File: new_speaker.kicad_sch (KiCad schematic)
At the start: 11 parts, among them J1 Conn_01x02, J2 Conn_01x04_Pin, J3 Conn_01x03_Pin, U1 MAX98357A

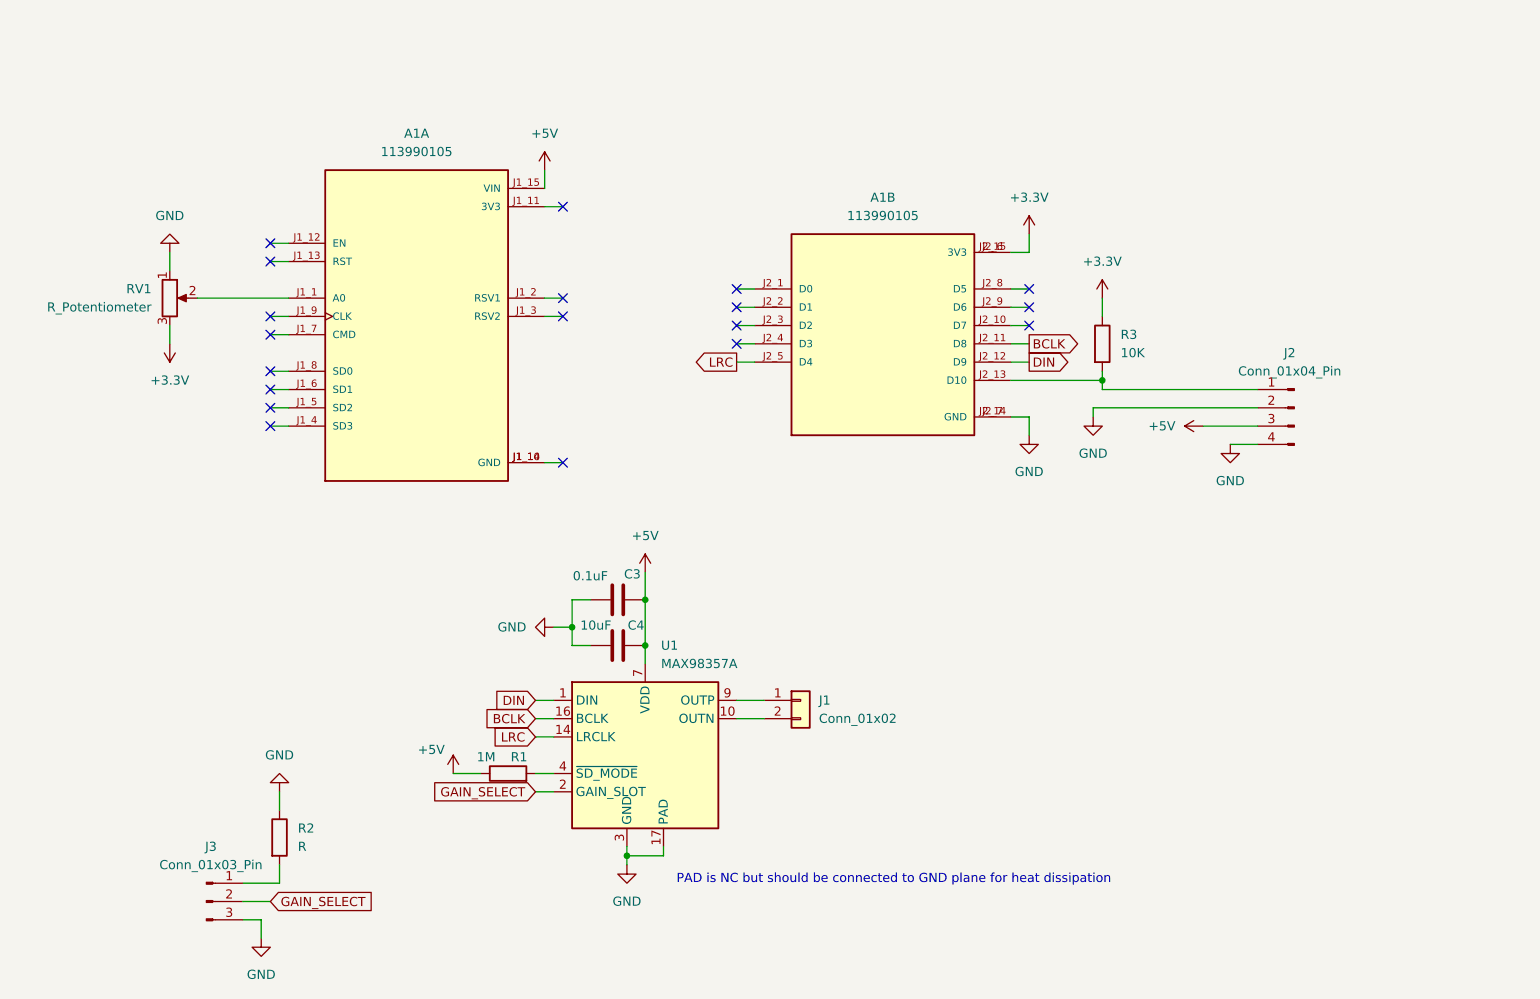
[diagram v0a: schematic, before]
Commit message: fixed nodemcu footprint
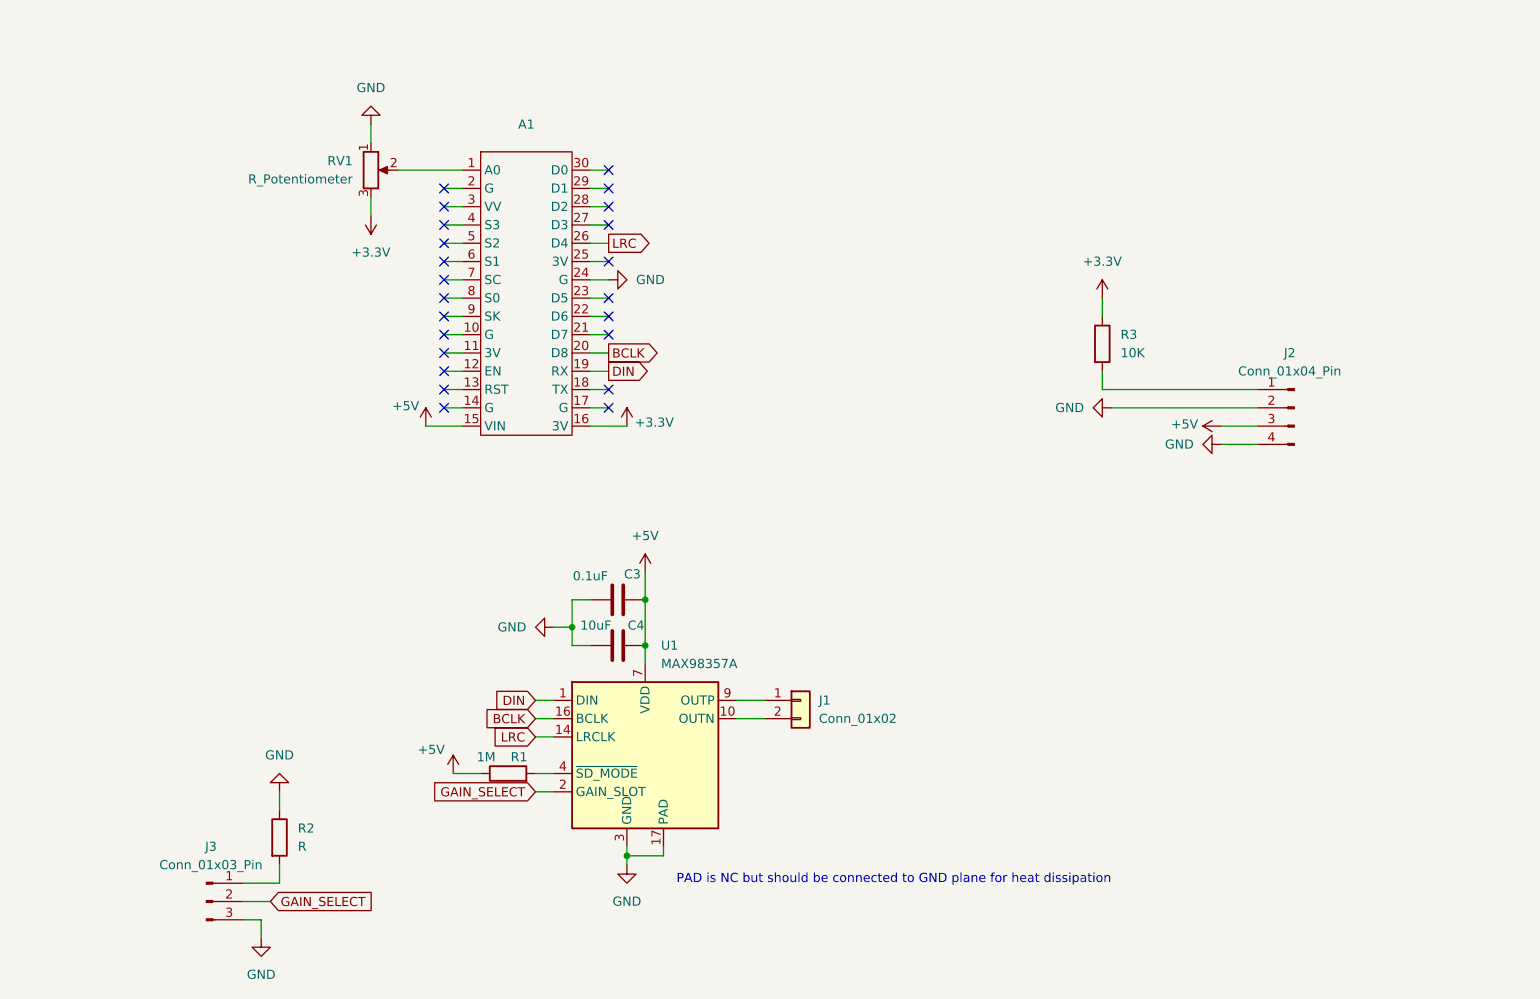
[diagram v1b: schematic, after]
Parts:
- removed A1: 113990105, footprints:SEEED_113990105, symbol nodemcu:113990105
- added A1: ~, footprints:NodeMCU-LoLinV3, symbol myfirstlib:my_esp8266_sym
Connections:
- net +3.3V: now also A1.16 (3V)
- net +5V: now also A1.15 (VIN)
- net BCLK: now also A1.20 (D8)
- net DIN: now also A1.19 (RX)
- net GND: now also A1.24 (G)
- net LRC: now also A1.26 (D4)
- net at RV1.2: now also A1.1 (A0)
- no-connect marks 19 -> 23
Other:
- moved on the sheet: RV1

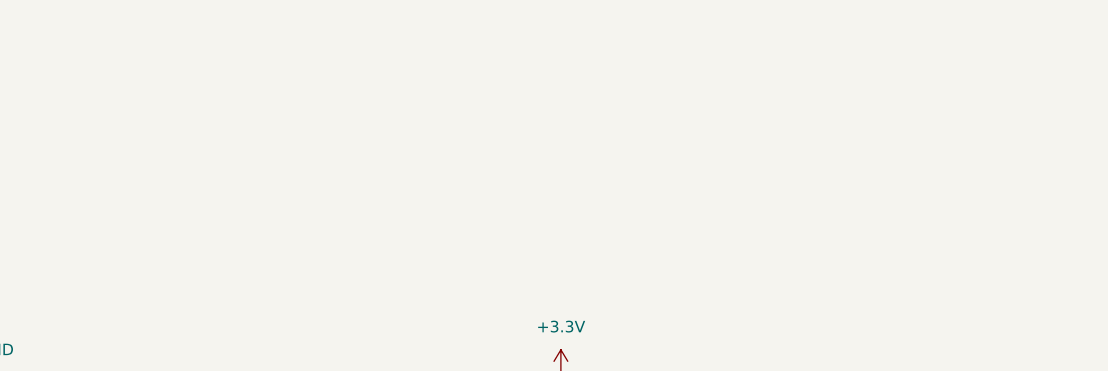
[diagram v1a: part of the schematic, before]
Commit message: added mounting pads and rounded corners
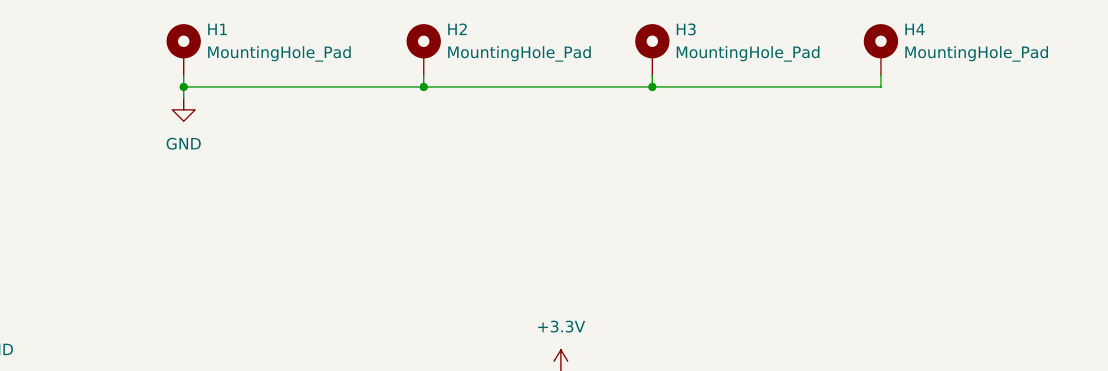
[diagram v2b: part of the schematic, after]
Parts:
- added H1, H2, H3, H4: MountingHole_Pad, MountingHole:MountingHole_3.2mm_M3_DIN965_Pad_TopBottom, symbol Mechanical:MountingHole_Pad
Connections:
- net GND: now also H1.1, H2.1, H3.1, H4.1

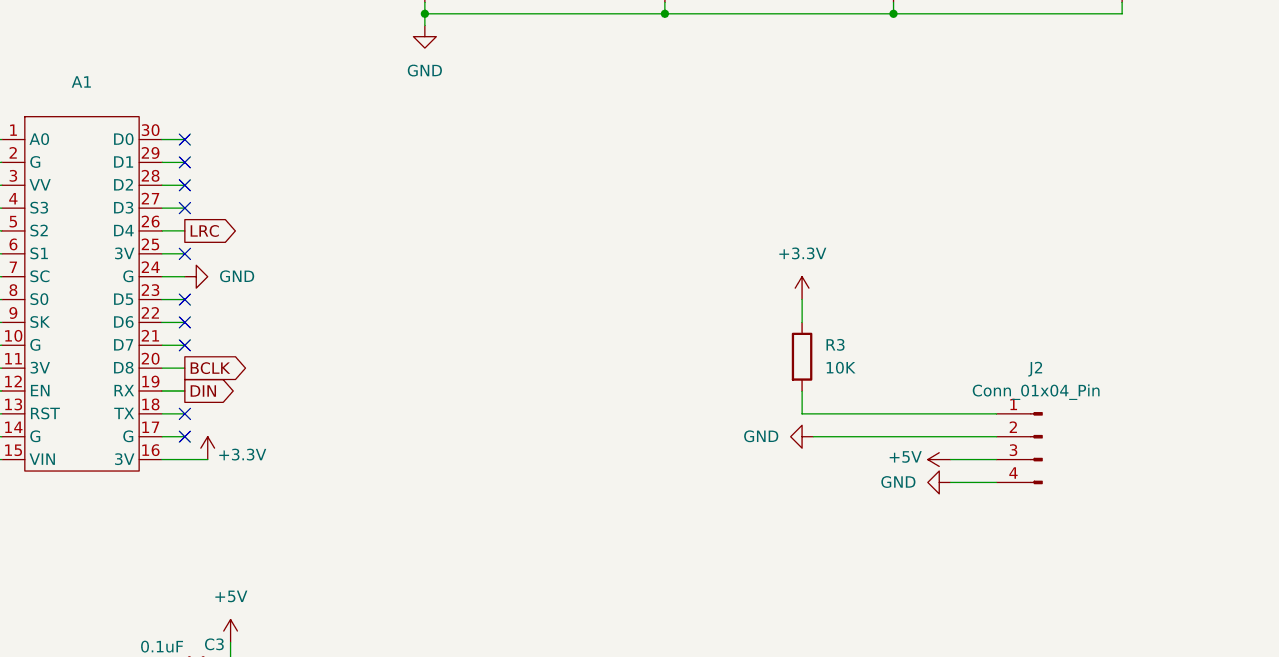
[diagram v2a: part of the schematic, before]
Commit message: fixed button input and added gain silkscreen
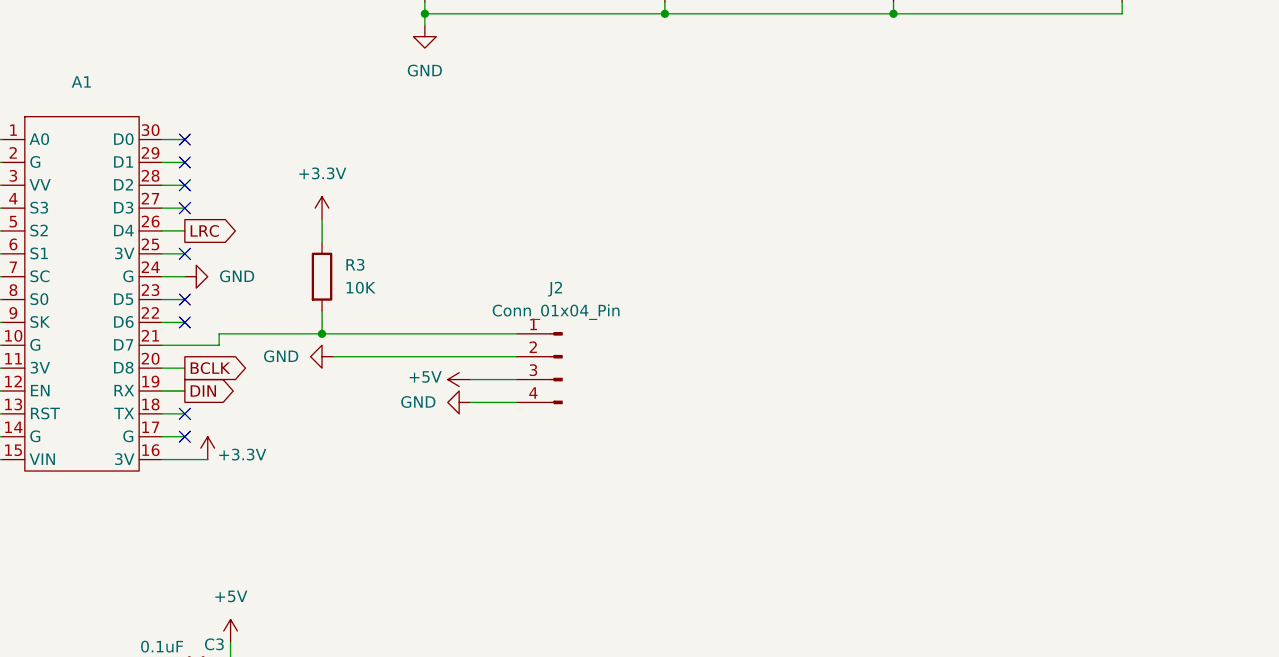
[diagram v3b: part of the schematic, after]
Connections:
- net at J2.1 (Pin_1), R3.2: now also A1.21 (D7)
- no-connect marks 23 -> 22
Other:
- moved on the sheet: J2, R3
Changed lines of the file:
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@@
+		(color 0 0 0 0)
+	)
+	(junction
+		(at 140.97 68.58)
+		(diameter 0)
 		(color 0 0 0 0)
 	)
@@
 	)
 	(no_connect
-		(at 125.73 69.85)
-	)
-	(no_connect
 		(at 102.87 62.23)
 	)
@@
 	(wire
 		(pts
-			(xy 194.31 64.77) (xy 194.31 67.31)
+			(xy 140.97 55.88) (xy 140.97 58.42)
 		)
 		(stroke
@@
 	(wire
 		(pts
-			(xy 210.82 82.55) (xy 215.9 82.55)
+			(xy 157.48 73.66) (xy 162.56 73.66)
 		)
 		(stroke
@@
 	(wire
 		(pts
-			(xy 194.31 74.93) (xy 194.31 77.47)
+			(xy 140.97 66.04) (xy 140.97 68.58)
 		)
 		(stroke
@@
 	(wire
 		(pts
-			(xy 195.58 80.01) (xy 215.9 80.01)
+			(xy 142.24 71.12) (xy 162.56 71.12)
 		)
 		(stroke
@@
 	(wire
 		(pts
-			(xy 123.19 69.85) (xy 125.73 69.85)
+			(xy 123.19 69.85) (xy 129.54 69.85)
 		)
 		(stroke
@@
 	(wire
 		(pts
+			(xy 129.54 69.85) (xy 129.54 68.58)
+		)
+		(stroke
+			(width 0)
+			(type default)
+		)
+	)
+	(wire
+		(pts
 			(xy 123.19 52.07) (xy 125.73 52.07)
 		)
@@
 	(wire
 		(pts
-			(xy 194.31 77.47) (xy 215.9 77.47)
+			(xy 140.97 68.58) (xy 162.56 68.58)
 		)
 		(stroke
@@
 	(wire
 		(pts
-			(xy 210.82 85.09) (xy 215.9 85.09)
+			(xy 157.48 76.2) (xy 162.56 76.2)
 		)
 		(stroke
@@
 		(pts
 			(xy 133.35 142.24) (xy 128.27 142.24)
+		)
+		(stroke
+			(width 0)
+			(type default)
+		)
+	)
+	(wire
+		(pts
+			(xy 129.54 68.58) (xy 140.97 68.58)
 		)
 		(stroke
@@
 	(symbol
 		(lib_id "power:GND")
-		(at 210.82 85.09 270)
+		(at 157.48 76.2 270)
 		(unit 1)
 		(exclude_from_sim no)
@@
 		(fields_autoplaced yes)
 		(property "Reference" "#PWR04"
-			(at 204.47 85.09 0)
+			(at 151.13 76.2 0)
 			(effects
 				(font
@@
 		)
 		(property "Value" "GND"
-			(at 207.01 85.0899 90)
+			(at 153.67 76.1999 90)
 			(effects
 				(font
@@
 		)
 		(property "Footprint" ""
-			(at 210.82 85.09 0)
+			(at 157.48 76.2 0)
 			(effects
 				(font
@@
 		)
 		(property "Datasheet" ""
-			(at 210.82 85.09 0)
+			(at 157.48 76.2 0)
 			(effects
 				(font
@@
 		)
 		(property "Description" "Power symbol creates a global label with name \"GND\" , ground"
-			(at 210.82 85.09 0)
+			(at 157.48 76.2 0)
 			(effects
 				(font
@@
 	(symbol
 		(lib_id "Device:R")
-		(at 194.31 71.12 0)
+		(at 140.97 62.23 0)
 		(unit 1)
 		(exclude_from_sim no)
@@
 		(fields_autoplaced yes)
 		(property "Reference" "R3"
-			(at 196.85 69.8499 0)
+			(at 143.51 60.9599 0)
 			(effects
 				(font
@@
 		)
 		(property "Value" "10K"
-			(at 196.85 72.3899 0)
+			(at 143.51 63.4999 0)
 			(effects
 				(font
@@
 		)
 		(property "Footprint" "Resistor_SMD:R_0805_2012Metric_Pad1.20x1.40mm_HandSolder"
-			(at 192.532 71.12 90)
+			(at 139.192 62.23 90)
 			(effects
 				(font
@@
 		)
 		(property "Datasheet" "~"
-			(at 194.31 71.12 0)
+			(at 140.97 62.23 0)
 			(effects
 				(font
@@
 		)
 		(property "Description" "Resistor"
-			(at 194.31 71.12 0)
+			(at 140.97 62.23 0)
 			(effects
 				(font
@@
 	(symbol
 		(lib_id "Connector:Conn_01x04_Pin")
-		(at 220.98 80.01 0)
+		(at 167.64 71.12 0)
 		(mirror y)
 		(unit 1)
@@
 		(dnp no)
 		(property "Reference" "J2"
-			(at 220.345 72.39 0)
+			(at 167.005 63.5 0)
 			(effects
 				(font
@@
 		)
 		(property "Value" "Conn_01x04_Pin"
-			(at 220.345 74.93 0)
+			(at 167.005 66.04 0)
 			(effects
 				(font
@@
 		)
 		(property "Footprint" "Connector_PinHeader_2.54mm:PinHeader_1x04_P2.54mm_Vertical"
-			(at 220.98 80.01 0)
+			(at 167.64 71.12 0)
 			(effects
 				(font
@@
 		)
 		(property "Datasheet" "~"
-			(at 220.98 80.01 0)
+			(at 167.64 71.12 0)
 			(effects
 				(font
@@
 		)
 		(property "Description" "Generic connector, single row, 01x04, script generated"
-			(at 220.98 80.01 0)
+			(at 167.64 71.12 0)
 			(effects
 				(font
@@
 	(symbol
 		(lib_id "power:+3.3V")
-		(at 194.31 64.77 0)
+		(at 140.97 55.88 0)
 		(unit 1)
 		(exclude_from_sim no)
@@
 		(fields_autoplaced yes)
 		(property "Reference" "#PWR012"
-			(at 194.31 68.58 0)
+			(at 140.97 59.69 0)
 			(effects
 				(font
@@
 		)
 		(property "Value" "+3.3V"
-			(at 194.31 59.69 0)
+			(at 140.97 50.8 0)
 			(effects
 				(font
@@
 		)
 		(property "Footprint" ""
-			(at 194.31 64.77 0)
+			(at 140.97 55.88 0)
 			(effects
 				(font
@@
 		)
 		(property "Datasheet" ""
-			(at 194.31 64.77 0)
+			(at 140.97 55.88 0)
 			(effects
 				(font
@@
 		)
 		(property "Description" "Power symbol creates a global label with name \"+3.3V\""
-			(at 194.31 64.77 0)
+			(at 140.97 55.88 0)
 			(effects
 				(font
@@
 	(symbol
 		(lib_id "power:GND")
-		(at 195.58 80.01 270)
+		(at 142.24 71.12 270)
 		(unit 1)
 		(exclude_from_sim no)
@@
 		(fields_autoplaced yes)
 		(property "Reference" "#PWR011"
-			(at 189.23 80.01 0)
+			(at 135.89 71.12 0)
 			(effects
 				(font
@@
 		)
 		(property "Value" "GND"
-			(at 191.77 80.0099 90)
+			(at 138.43 71.1199 90)
 			(effects
 				(font
@@
 		)
 		(property "Footprint" ""
-			(at 195.58 80.01 0)
+			(at 142.24 71.12 0)
 			(effects
 				(font
@@
 		)
 		(property "Datasheet" ""
-			(at 195.58 80.01 0)
+			(at 142.24 71.12 0)
 			(effects
 				(font
@@
 		)
 		(property "Description" "Power symbol creates a global label with name \"GND\" , ground"
-			(at 195.58 80.01 0)
+			(at 142.24 71.12 0)
 			(effects
 				(font
@@
 	(symbol
 		(lib_id "power:+5V")
-		(at 210.82 82.55 90)
+		(at 157.48 73.66 90)
 		(unit 1)
 		(exclude_from_sim no)
@@
 		(dnp no)
 		(property "Reference" "#PWR013"
-			(at 214.63 82.55 0)
+			(at 161.29 73.66 0)
 			(effects
 				(font
@@
 		)
 		(property "Value" "+5V"
-			(at 205.74 82.296 90)
+			(at 152.4 73.406 90)
 			(effects
 				(font
@@
 		)
 		(property "Footprint" ""
-			(at 210.82 82.55 0)
+			(at 157.48 73.66 0)
 			(effects
 				(font
@@
 		)
 		(property "Datasheet" ""
-			(at 210.82 82.55 0)
+			(at 157.48 73.66 0)
 			(effects
 				(font
@@
 		)
 		(property "Description" "Power symbol creates a global label with name \"+5V\""
-			(at 210.82 82.55 0)
-			(effects
-				(font
+			(at 157.48 73.66 0)
+			(effects
+				(font

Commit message: updated resistor value in sch
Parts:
- R2: value R -> 100K
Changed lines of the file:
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@@
 			)
 		)
-		(property "Value" "R"
+		(property "Value" "100K"
 			(at 82.55 140.9699 0)
 			(effects
